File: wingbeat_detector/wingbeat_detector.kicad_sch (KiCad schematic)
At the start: 0 parts

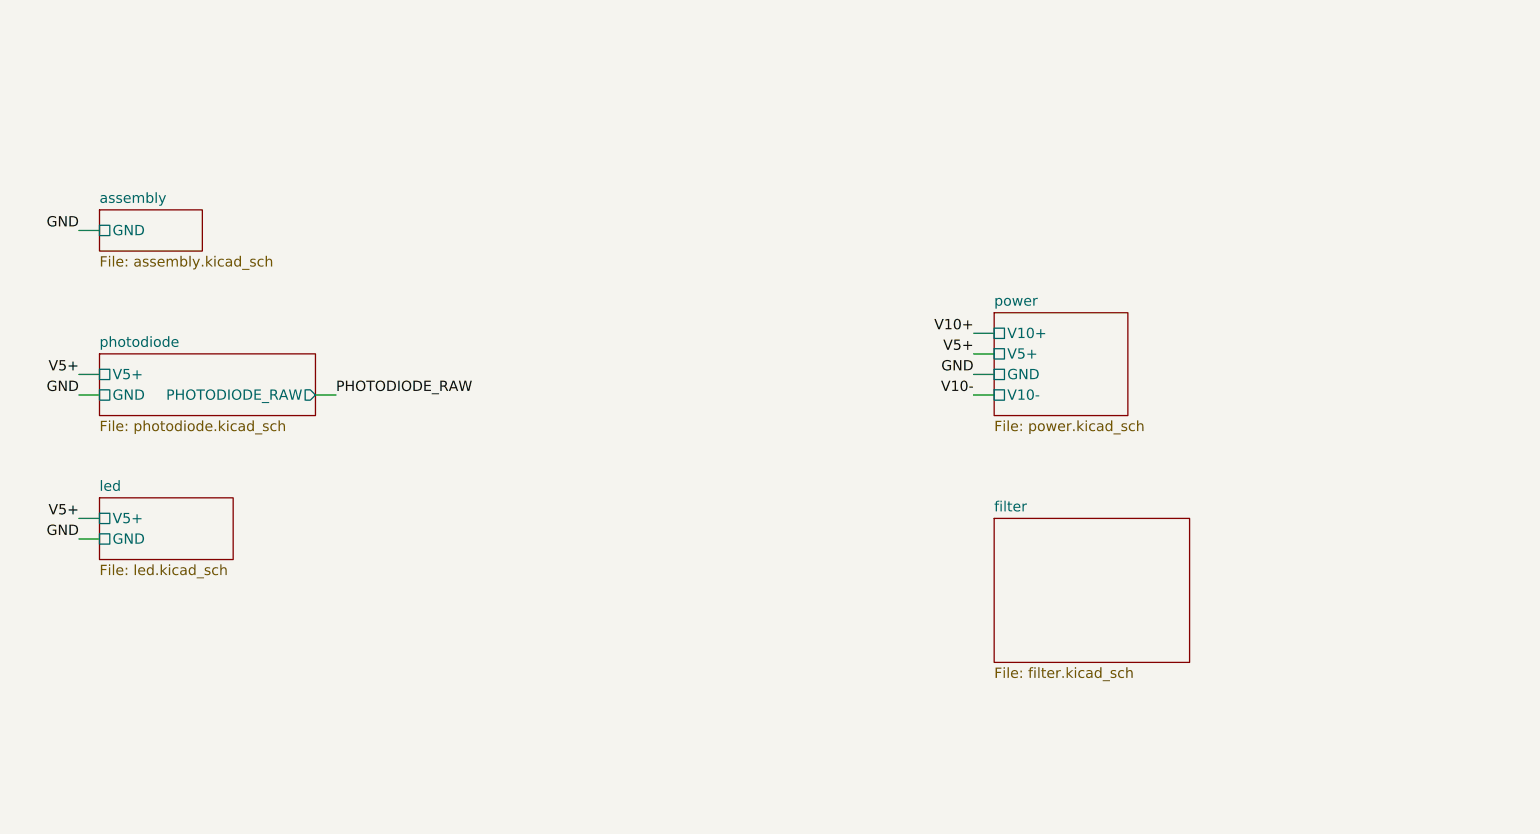
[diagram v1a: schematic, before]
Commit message: Initial schematic layout
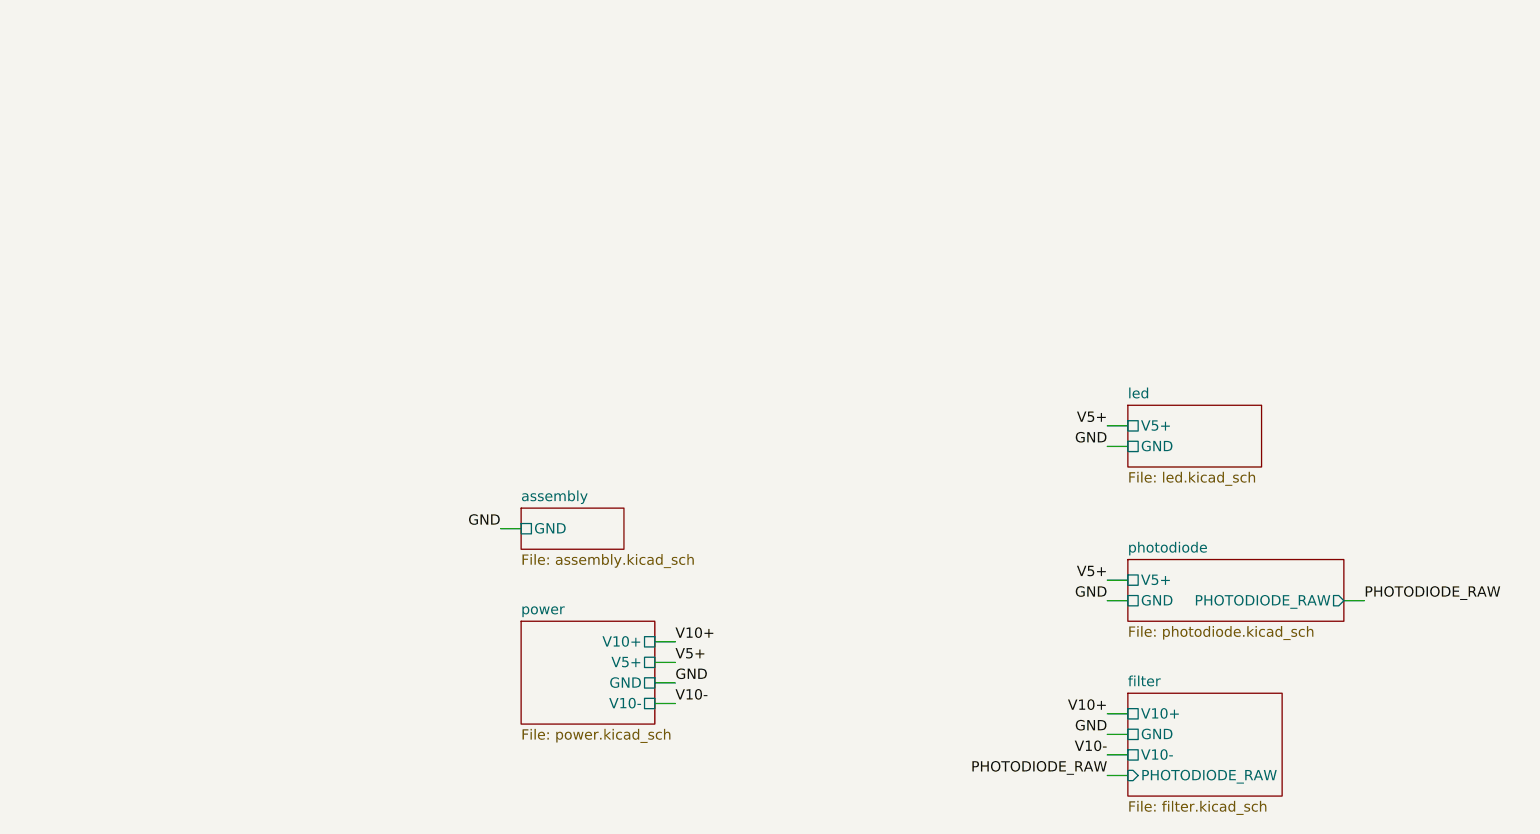
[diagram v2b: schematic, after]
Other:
- sheet filter ports: added GND, PHOTODIODE_RAW, V10+, V10-; removed none
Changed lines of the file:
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@@
     (company "Howard Hughes Medical Institute")
   )
-  (wire (pts (xy 39.37 88.9) (xy 41.91 88.9))
+  (wire (pts (xy 166.37 77.47) (xy 168.91 77.47))
     (stroke (width 0) (type default))
   )
-  (wire (pts (xy 39.37 91.44) (xy 41.91 91.44))
+  (wire (pts (xy 166.37 80.01) (xy 168.91 80.01))
     (stroke (width 0) (type default))
   )
-  (wire (pts (xy 149.86 73.66) (xy 152.4 73.66))
+  (wire (pts (xy 113.03 111.76) (xy 110.49 111.76))
     (stroke (width 0) (type default))
   )
-  (wire (pts (xy 39.37 73.66) (xy 41.91 73.66))
+  (wire (pts (xy 166.37 120.65) (xy 168.91 120.65))
     (stroke (width 0) (type default))
   )
-  (wire (pts (xy 39.37 71.12) (xy 41.91 71.12))
+  (wire (pts (xy 166.37 99.06) (xy 168.91 99.06))
     (stroke (width 0) (type default))
   )
-  (wire (pts (xy 149.86 71.12) (xy 152.4 71.12))
+  (wire (pts (xy 166.37 96.52) (xy 168.91 96.52))
     (stroke (width 0) (type default))
   )
-  (wire (pts (xy 39.37 53.34) (xy 41.91 53.34))
+  (wire (pts (xy 113.03 109.22) (xy 110.49 109.22))
     (stroke (width 0) (type default))
   )
-  (wire (pts (xy 149.86 66.04) (xy 152.4 66.04))
+  (wire (pts (xy 166.37 118.11) (xy 168.91 118.11))
     (stroke (width 0) (type default))
   )
-  (wire (pts (xy 71.12 73.66) (xy 68.58 73.66))
+  (wire (pts (xy 91.44 90.17) (xy 93.98 90.17))
     (stroke (width 0) (type default))
   )
-  (wire (pts (xy 149.86 68.58) (xy 152.4 68.58))
+  (wire (pts (xy 166.37 113.03) (xy 168.91 113.03))
     (stroke (width 0) (type default))
   )
-  (label "V10-" (at 149.86 73.66 180) (fields_autoplaced)
+  (wire (pts (xy 113.03 104.14) (xy 110.49 104.14))
+    (stroke (width 0) (type default))
+  )
+  (wire (pts (xy 198.12 99.06) (xy 195.58 99.06))
+    (stroke (width 0) (type default))
+  )
+  (wire (pts (xy 166.37 115.57) (xy 168.91 115.57))
+    (stroke (width 0) (type default))
+  )
+  (wire (pts (xy 110.49 106.68) (xy 113.03 106.68))
+    (stroke (width 0) (type default))
+  )
+  (label "V10-" (at 113.03 111.76 0) (fields_autoplaced)
+    (effects (font (size 1.27 1.27)) (justify left bottom))
+  )
+  (label "GND" (at 113.03 109.22 0) (fields_autoplaced)
+    (effects (font (size 1.27 1.27)) (justify left bottom))
+  )
+  (label "V10+" (at 166.37 113.03 180) (fields_autoplaced)
     (effects (font (size 1.27 1.27)) (justify right bottom))
   )
-  (label "GND" (at 149.86 71.12 180) (fields_autoplaced)
+  (label "GND" (at 91.44 90.17 180) (fields_autoplaced)
     (effects (font (size 1.27 1.27)) (justify right bottom))
   )
-  (label "GND" (at 39.37 53.34 180) (fields_autoplaced)
+  (label "GND" (at 166.37 80.01 180) (fields_autoplaced)
     (effects (font (size 1.27 1.27)) (justify right bottom))
   )
-  (label "GND" (at 39.37 91.44 180) (fields_autoplaced)
+  (label "GND" (at 166.37 99.06 180) (fields_autoplaced)
     (effects (font (size 1.27 1.27)) (justify right bottom))
   )
-  (label "GND" (at 39.37 73.66 180) (fields_autoplaced)
+  (label "V10+" (at 113.03 104.14 0) (fields_autoplaced)
+    (effects (font (size 1.27 1.27)) (justify left bottom))
+  )
+  (label "V5+" (at 166.37 96.52 180) (fields_autoplaced)
     (effects (font (size 1.27 1.27)) (justify right bottom))
   )
-  (label "V10+" (at 149.86 66.04 180) (fields_autoplaced)
+  (label "V5+" (at 113.03 106.68 0) (fields_autoplaced)
+    (effects (font (size 1.27 1.27)) (justify left bottom))
+  )
+  (label "V5+" (at 166.37 77.47 180) (fields_autoplaced)
     (effects (font (size 1.27 1.27)) (justify right bottom))
   )
-  (label "V5+" (at 39.37 71.12 180) (fields_autoplaced)
+  (label "PHOTODIODE_RAW" (at 198.12 99.06 0) (fields_autoplaced)
+    (effects (font (size 1.27 1.27)) (justify left bottom))
+  )
+  (label "GND" (at 166.37 115.57 180) (fields_autoplaced)
     (effects (font (size 1.27 1.27)) (justify right bottom))
   )
-  (label "V5+" (at 149.86 68.58 180) (fields_autoplaced)
+  (label "PHOTODIODE_RAW" (at 166.37 120.65 180) (fields_autoplaced)
     (effects (font (size 1.27 1.27)) (justify right bottom))
   )
-  (label "V5+" (at 39.37 88.9 180) (fields_autoplaced)
+  (label "V10-" (at 166.37 118.11 180) (fields_autoplaced)
     (effects (font (size 1.27 1.27)) (justify right bottom))
   )
-  (label "PHOTODIODE_RAW" (at 71.12 73.66 0) (fields_autoplaced)
-    (effects (font (size 1.27 1.27)) (justify left bottom))
-  )
-  (sheet (at 41.91 50.8) (size 12.7 5.08) (fields_autoplaced)
+  (sheet (at 93.98 87.63) (size 12.7 5.08) (fields_autoplaced)
     (stroke (width 0.1524) (type solid))
     (fill (color 0 0 0 0.0000))
-    (property "Sheetname" "assembly" (at 41.91 50.0884 0)
+    (property "Sheetname" "assembly" (at 93.98 86.9184 0)
       (effects (font (size 1.27 1.27)) (justify left bottom))
     )
-    (property "Sheetfile" "assembly.kicad_sch" (at 41.91 56.4646 0)
+    (property "Sheetfile" "assembly.kicad_sch" (at 93.98 93.2946 0)
       (effects (font (size 1.27 1.27)) (justify left top))
     )
-    (pin "GND" passive (at 41.91 53.34 180)
+    (pin "GND" passive (at 93.98 90.17 180)
       (effects (font (size 1.27 1.27)) (justify left))
     )
@@
     )
   )
-  (sheet (at 41.91 86.36) (size 16.51 7.62) (fields_autoplaced)
+  (sheet (at 168.91 74.93) (size 16.51 7.62) (fields_autoplaced)
     (stroke (width 0.1524) (type solid))
     (fill (color 0 0 0 0.0000))
-    (property "Sheetname" "led" (at 41.91 85.6484 0)
+    (property "Sheetname" "led" (at 168.91 74.2184 0)
       (effects (font (size 1.27 1.27)) (justify left bottom))
     )
-    (property "Sheetfile" "led.kicad_sch" (at 41.91 94.5646 0)
+    (property "Sheetfile" "led.kicad_sch" (at 168.91 83.1346 0)
       (effects (font (size 1.27 1.27)) (justify left top))
     )
-    (pin "GND" passive (at 41.91 91.44 180)
+    (pin "GND" passive (at 168.91 80.01 180)
       (effects (font (size 1.27 1.27)) (justify left))
     )
-    (pin "V5+" passive (at 41.91 88.9 180)
+    (pin "V5+" passive (at 168.91 77.47 180)
       (effects (font (size 1.27 1.27)) (justify left))
     )
@@
     )
   )
-  (sheet (at 152.4 88.9) (size 24.13 17.78) (fields_autoplaced)
+  (sheet (at 168.91 110.49) (size 19.05 12.7) (fields_autoplaced)
     (stroke (width 0.1524) (type solid))
     (fill (color 0 0 0 0.0000))
-    (property "Sheetname" "filter" (at 152.4 88.1884 0)
+    (property "Sheetname" "filter" (at 168.91 109.7784 0)
       (effects (font (size 1.27 1.27)) (justify left bottom))
     )
-    (property "Sheetfile" "filter.kicad_sch" (at 152.4 107.2646 0)
+    (property "Sheetfile" "filter.kicad_sch" (at 168.91 123.7746 0)
       (effects (font (size 1.27 1.27)) (justify left top))
+    )
+    (pin "V10-" passive (at 168.91 118.11 180)
+      (effects (font (size 1.27 1.27)) (justify left))
+    )
+    (pin "PHOTODIODE_RAW" input (at 168.91 120.65 180)
+      (effects (font (size 1.27 1.27)) (justify left))
+    )
+    (pin "V10+" passive (at 168.91 113.03 180)
+      (effects (font (size 1.27 1.27)) (justify left))
+    )
+    (pin "GND" passive (at 168.91 115.57 180)
+      (effects (font (size 1.27 1.27)) (justify left))
     )
     (instances
@@
     )
   )
-  (sheet (at 152.4 63.5) (size 16.51 12.7) (fields_autoplaced)
+  (sheet (at 93.98 101.6) (size 16.51 12.7) (fields_autoplaced)
     (stroke (width 0.1524) (type solid))
     (fill (color 0 0 0 0.0000))
-    (property "Sheetname" "power" (at 152.4 62.7884 0)
+    (property "Sheetname" "power" (at 93.98 100.8884 0)
       (effects (font (size 1.27 1.27)) (justify left bottom))
     )
-    (property "Sheetfile" "power.kicad_sch" (at 152.4 76.7846 0)
+    (property "Sheetfile" "power.kicad_sch" (at 93.98 114.8846 0)
       (effects (font (size 1.27 1.27)) (justify left top))
     )
-    (pin "GND" passive (at 152.4 71.12 180)
-      (effects (font (size 1.27 1.27)) (justify left))
+    (pin "GND" passive (at 110.49 109.22 0)
+      (effects (font (size 1.27 1.27)) (justify right))
     )
-    (pin "V5+" passive (at 152.4 68.58 180)
-      (effects (font (size 1.27 1.27)) (justify left))
+    (pin "V5+" passive (at 110.49 106.68 0)
+      (effects (font (size 1.27 1.27)) (justify right))
     )
-    (pin "V10+" passive (at 152.4 66.04 180)
-      (effects (font (size 1.27 1.27)) (justify left))
+    (pin "V10+" passive (at 110.49 104.14 0)
+      (effects (font (size 1.27 1.27)) (justify right))
     )
-    (pin "V10-" passive (at 152.4 73.66 180)
-      (effects (font (size 1.27 1.27)) (justify left))
+    (pin "V10-" passive (at 110.49 111.76 0)
+      (effects (font (size 1.27 1.27)) (justify right))
     )
     (instances
@@
     )
   )
-  (sheet (at 41.91 68.58) (size 26.67 7.62) (fields_autoplaced)
+  (sheet (at 168.91 93.98) (size 26.67 7.62) (fields_autoplaced)
     (stroke (width 0.1524) (type solid))
     (fill (color 0 0 0 0.0000))
-    (property "Sheetname" "photodiode" (at 41.91 67.8684 0)
+    (property "Sheetname" "photodiode" (at 168.91 93.2684 0)
       (effects (font (size 1.27 1.27)) (justify left bottom))
     )
-    (property "Sheetfile" "photodiode.kicad_sch" (at 41.91 76.7846 0)
+    (property "Sheetfile" "photodiode.kicad_sch" (at 168.91 102.1846 0)
       (effects (font (size 1.27 1.27)) (justify left top))
     )
-    (pin "V5+" passive (at 41.91 71.12 180)
+    (pin "V5+" passive (at 168.91 96.52 180)
       (effects (font (size 1.27 1.27)) (justify left))
     )
-    (pin "GND" passive (at 41.91 73.66 180)
+    (pin "GND" passive (at 168.91 99.06 180)
       (effects (font (size 1.27 1.27)) (justify left))
     )
-    (pin "PHOTODIODE_RAW" output (at 68.58 73.66 0)
+    (pin "PHOTODIODE_RAW" output (at 195.58 99.06 0)
       (effects (font (size 1.27 1.27)) (justify right))
     )

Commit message: Double check schematic
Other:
- sheet photodiode ports: added V10-; removed none
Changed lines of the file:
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@@
+    (stroke (width 0) (type default))
+  )
+  (wire (pts (xy 166.37 101.6) (xy 168.91 101.6))
     (stroke (width 0) (type default))
   )
@@
     (effects (font (size 1.27 1.27)) (justify right bottom))
   )
+  (label "V10-" (at 166.37 101.6 180) (fields_autoplaced)
+    (effects (font (size 1.27 1.27)) (justify right bottom))
+  )
   (label "GND" (at 166.37 80.01 180) (fields_autoplaced)
     (effects (font (size 1.27 1.27)) (justify right bottom))
@@
     )
   )
-  (sheet (at 168.91 93.98) (size 26.67 7.62) (fields_autoplaced)
+  (sheet (at 168.91 93.98) (size 26.67 10.16) (fields_autoplaced)
     (stroke (width 0.1524) (type solid))
     (fill (color 0 0 0 0.0000))
@@
       (effects (font (size 1.27 1.27)) (justify left bottom))
     )
-    (property "Sheetfile" "photodiode.kicad_sch" (at 168.91 102.1846 0)
+    (property "Sheetfile" "photodiode.kicad_sch" (at 168.91 104.7246 0)
       (effects (font (size 1.27 1.27)) (justify left top))
     )
@@
       (effects (font (size 1.27 1.27)) (justify right))
     )
-    (instances
+    (pin "V10-" passive (at 168.91 101.6 180)
+      (effects (font (size 1.27 1.27)) (justify left))
+    )
+    (instances

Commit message: Finished layout for v3.0
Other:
- company: Howard Hughes Medical Institute -> Peter Polidoro
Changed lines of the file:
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@@
   (title_block
     (title "wingbeat_detector")
-    (date "2023-03-22")
+    (date "2023-03-23")
     (rev "3.0")
-    (company "Howard Hughes Medical Institute")
+    (company "Peter Polidoro")
   )
   (wire (pts (xy 166.37 77.47) (xy 168.91 77.47))
